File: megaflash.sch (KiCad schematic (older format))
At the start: 26 parts, among them J1 ROM7, J2 ROM0, J3 CPC_EXTPORT, U1 74LS374, U2 74LS32, U3 74LS32, U4 74LS02, U5 74LS20, U6 W29C040

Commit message: Nearly finished layout, tweaks/fixes on schematic.
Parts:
- R1: renamed from 1K1; value R -> 1K
- gave numbers to parts that had none: 1
- renumbered U3 to U2, U2 to U3
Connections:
- net labels added: ~CE, ~IORQ, ~MREQ, ~ROM0DECODE, ~ROM0SEL, ~ROM7DECODE, ~ROM7SEL, ~ROMEN, ~WR, ~WREN
- net labels removed: /CE, /ROM0DECODE, /ROM0SEL, /ROM7DECODE, /ROM7SEL, IORQ, MREQ, ROMEN, WR, WREN
- wire segments 156 -> 159
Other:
- note added: "~ROM0DECODE~ <- A14+A15+A16+A17+A18 (&0000-&3FFF)\n~ROM7DECODE~ <- ~A14~+~A15~+~A16~+A17+A18 (&1C000-&1FFFF)"
- note removed: "/ROM0DECODE <- A14+A15+A16+A17+A18 (&0000-&3FFF)\n/ROM7DECODE <- !A14+!A15+!A16+A17+A18 (&1C000-&1FFFF)"
- moved on the sheet: U3A, U3B

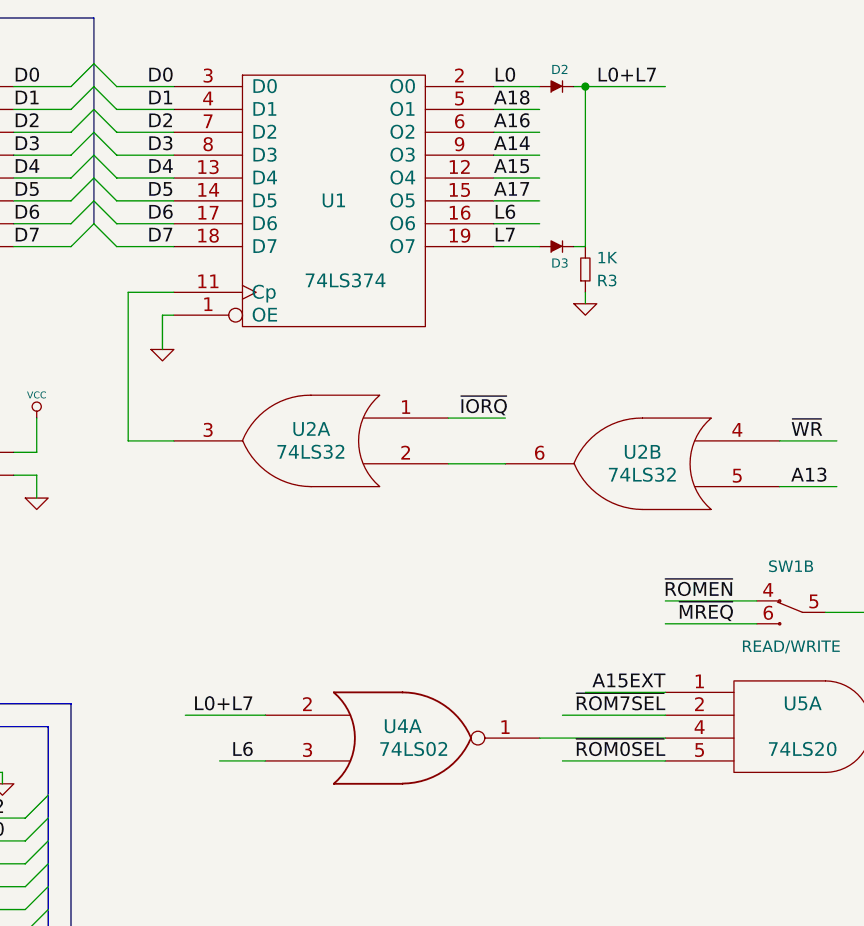
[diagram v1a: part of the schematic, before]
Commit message: Fixed scrambled latch inputs. Board mostly routed.
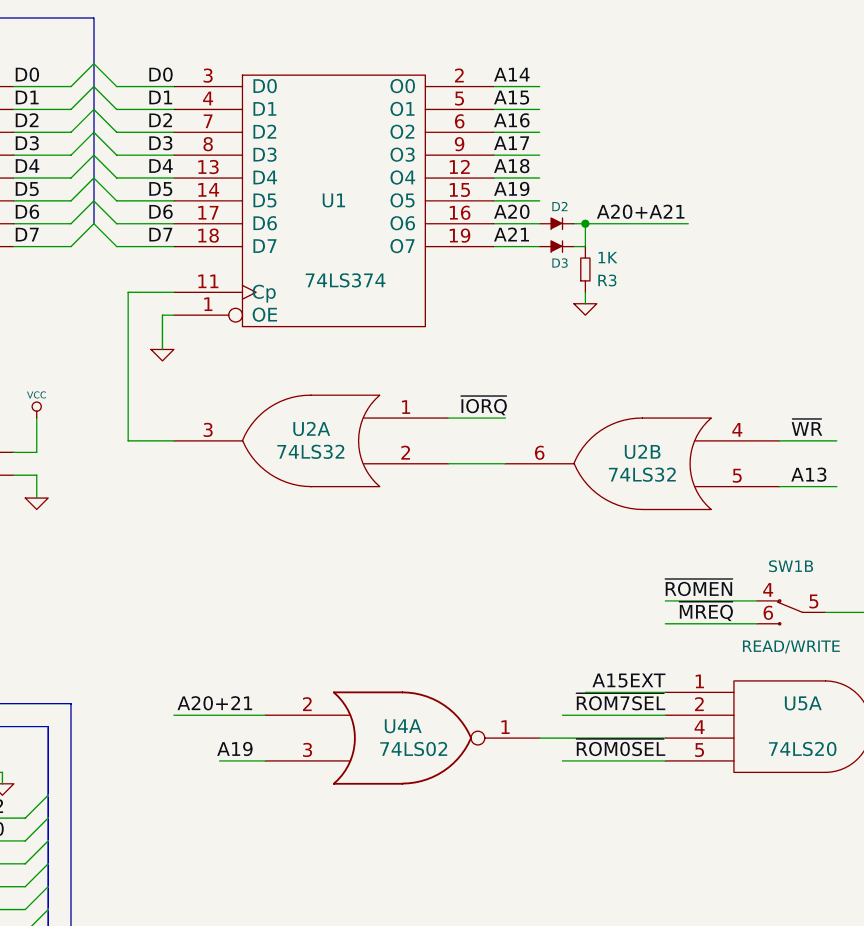
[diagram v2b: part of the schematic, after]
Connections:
- net labels added: A19, A20, A20+21, A20+A21, A21
- net labels removed: L0, L0+L7, L6, L7
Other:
- moved on the sheet: D2
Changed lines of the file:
@@
 A15EXT
 Text Label 5100 1150 0    60   ~ 0
-L0
+A14
 Text Label 5100 1250 0    60   ~ 0
-A18
+A15
 Text Label 5100 1350 0    60   ~ 0
 A16
 Text Label 5100 1450 0    60   ~ 0
-A14
+A17
 Text Label 5100 1550 0    60   ~ 0
-A15
+A18
 Text Label 5100 1650 0    60   ~ 0
-A17
+A19
 Text Label 5100 1750 0    60   ~ 0
-L6
+A20
 Text Label 5100 1850 0    60   ~ 0
-L7
+A21
 Text Label 5400 5000 2    60   ~ 0
 A17
@@
 A17
 Text Label 4050 4100 2    60   ~ 0
-L6
+A19
 Text Label 4050 3900 2    60   ~ 0
-L0+L7
+A20+21
 $Comp
 L DIODE D2
 U 1 1 534FD423
-P 5350 1150
-F 0 "D2" H 5350 1200 40  0000 L BNN
-F 1 "DIODE" H 5350 1050 40  0001 C CNN
-F 2 "" H 5350 1150 60  0000 C CNN
-F 3 "" H 5350 1150 60  0000 C CNN
-	1    5350 1150
+P 5350 1750
+F 0 "D2" H 5350 1800 40  0000 L BNN
+F 1 "DIODE" H 5350 1650 40  0001 C CNN
+F 2 "" H 5350 1750 60  0000 C CNN
+F 3 "" H 5350 1750 60  0000 C CNN
+	1    5350 1750
 	1    0    0    -1
 $EndComp
@@
 	1    0    0    -1
 $EndComp
-Text Label 5550 1150 0    60   ~ 0
-L0+L7
+Text Label 5550 1750 0    60   ~ 0
+A20+A21
 $Comp
 L R R3
@@
 	4100 4100 3900 4100
 Wire Wire Line
-	3750 3900 4100 3900
+	3700 3900 4100 3900
 Wire Wire Line
 	5450 1850 5500 1850
-Wire Wire Line
-	5500 1850 5500 1150
-Wire Wire Line
-	5450 1150 5850 1150
-Connection ~ 5500 1150
 Wire Wire Line
 	6650 5600 6850 5600
@@
 Wire Wire Line
 	2950 4150 2950 4200
-Wire Wire Line
-	4850 6950 4700 6950
 $Comp
 L LED LD1
@@
 Connection ~ 8900 1350
 Connection ~ 9200 1350
+Wire Wire Line
+	4850 6950 4700 6950
+Wire Wire Line
+	5500 1850 5500 1750
+Wire Wire Line
+	5450 1750 5950 1750
+Connection ~ 5500 1750
 $EndSCHEMATC

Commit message: Completed v1 schematic and layout using XC9536 cpld.
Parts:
- removed C1: 100u, symbol C
- removed C6, C7, C8: 100n, symbol C
- removed J1: ROM7, symbol HEADER_3
- removed J2: ROM0, symbol HEADER_3
- removed R4: 1K, symbol R
- removed SW1: READ/WRITE, symbol SW_DPDT
- removed U1: 74LS374, symbol 74LS374
- removed U2, U3: 74LS32, symbol 74LS32
- removed U4: 74LS02, symbol 74LS02
- removed U5: 74LS20, symbol 74LS20
- added C1: 100u, symbol CAP
- added C4: 10n, symbol C
- added J2: PROG, symbol HEADER_2X2
- added J3: JTAG, symbol HEADER_6
- added SW1: ~READ~/WRITE, symbol SWITCH_INV
- added SW2: ROM0ENABLE, symbol SWITCH_INV
- added SW3: ROM7ENABLE, symbol SWITCH_INV
- added U2: XC9536PC44, symbol XC9536PC44
- C2: renamed from C3; value 100n -> 10n
- C3: renamed from C4; value 100n -> 10n
- C5: value 100n -> 10n
- R2: value 220 -> 10k
- R3: value 1K -> 1k
- U1: renamed from U6; value W29C040 -> W29C040 or SST39V040
- renumbered J3 to J1
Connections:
- net labels added: A14EXT, CLK, ROM0EN, ROM7EN, ~RD, ~RD~WR
- net labels removed: A19, A20, A20+21, A20+A21, A21, ~ROM0DECODE, ~ROM0SEL, ~ROM7DECODE, ~ROM7SEL
- wire segments 159 -> 144
- no-connect marks 20 -> 16
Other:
- note removed: "~ROM0DECODE~ <- A14+A15+A16+A17+A18 (&0000-&3FFF)\n~ROM7DECODE~ <- ~A14~+~A15~+~A16~+A17+A18 (&1C000-&1FFFF)"
- moved on the sheet: C2, C3

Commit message: Replaced switch with one that's available from digikey.
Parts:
- added R4: 10k, symbol R
- R1: value 1K -> 1k
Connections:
- wire segments 144 -> 146
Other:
- moved on the sheet: LD1, R3
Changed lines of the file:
@@
 ~ROMEN
 $Comp
-L GND #PWR01
+L GND #PWR6
 U 1 1 534FA3BF
 P 3100 2950
-F 0 "#PWR01" H 3100 2950 30  0001 C CNN
+F 0 "#PWR6" H 3100 2950 30  0001 C CNN
 F 1 "GND" H 3100 2880 30  0001 C CNN
 F 2 "" H 3100 2950 60  0000 C CNN
@@
 $EndComp
 $Comp
-L VCC #PWR02
+L VCC #PWR5
 U 1 1 534FA42A
 P 3100 2600
-F 0 "#PWR02" H 3100 2700 30  0001 C CNN
+F 0 "#PWR5" H 3100 2700 30  0001 C CNN
 F 1 "VCC" H 3100 2700 30  0000 C CNN
 F 2 "" H 3100 2600 60  0000 C CNN
@@
 P 1400 6000
 F 0 "R1" H 1350 5950 50  0000 R CNN
-F 1 "1K" H 1350 6050 50  0000 R CNN
+F 1 "1k" H 1350 6050 50  0000 R CNN
 F 2 "" H 1400 6000 60  0000 C CNN
 F 3 "" H 1400 6000 60  0000 C CNN
@@
 ROMDIS
 $Comp
-L VCC #PWR03
+L VCC #PWR1
 U 1 1 534FE519
 P 1250 5550
-F 0 "#PWR03" H 1250 5650 30  0001 C CNN
+F 0 "#PWR1" H 1250 5650 30  0001 C CNN
 F 1 "VCC" H 1250 5650 30  0000 C CNN
 F 2 "" H 1250 5550 60  0000 C CNN
@@
 NoConn ~ 1800 5550
 $Comp
-L GND #PWR04
+L GND #PWR3
 U 1 1 534FFC5A
 P 1800 6600
-F 0 "#PWR04" H 1800 6600 30  0001 C CNN
+F 0 "#PWR3" H 1800 6600 30  0001 C CNN
 F 1 "GND" H 1800 6530 30  0001 C CNN
 F 2 "" H 1800 6600 60  0000 C CNN
@@
 $EndComp
 $Comp
-L GND #PWR05
+L GND #PWR4
 U 1 1 534FFDA2
 P 2950 4100
-F 0 "#PWR05" H 2950 4100 30  0001 C CNN
+F 0 "#PWR4" H 2950 4100 30  0001 C CNN
 F 1 "GND" H 2950 4030 30  0001 C CNN
 F 2 "" H 2950 4100 60  0000 C CNN
@@
 $EndComp
 $Comp
-L GND #PWR06
+L GND #PWR2
 U 1 1 53501BF6
 P 1250 5800
-F 0 "#PWR06" H 1250 5800 30  0001 C CNN
+F 0 "#PWR2" H 1250 5800 30  0001 C CNN
 F 1 "GND" H 1250 5730 30  0001 C CNN
 F 2 "" H 1250 5800 60  0000 C CNN
@@
 $EndComp
 $Comp
-L GND #PWR07
+L GND #PWR10
 U 1 1 535025BB
 P 6950 1750
-F 0 "#PWR07" H 6950 1750 30  0001 C CNN
+F 0 "#PWR10" H 6950 1750 30  0001 C CNN
 F 1 "GND" H 6950 1680 30  0001 C CNN
 F 2 "" H 6950 1750 60  0000 C CNN
@@
 $EndComp
 $Comp
-L GND #PWR08
+L GND #PWR8
 U 1 1 535363D7
 P 6400 5400
-F 0 "#PWR08" H 6400 5400 30  0001 C CNN
+F 0 "#PWR8" H 6400 5400 30  0001 C CNN
 F 1 "GND" H 6400 5330 30  0001 C CNN
 F 2 "" H 6400 5400 60  0000 C CNN
@@
 ROM7EN
 $Comp
-L GND #PWR09
+L GND #PWR16
 U 1 1 5353B454
 P 10550 2900
-F 0 "#PWR09" H 10550 2900 30  0001 C CNN
+F 0 "#PWR16" H 10550 2900 30  0001 C CNN
 F 1 "GND" H 10550 2830 30  0001 C CNN
 F 2 "" H 10550 2900 60  0000 C CNN
@@
 $EndComp
 $Comp
-L VCC #PWR010
+L VCC #PWR17
 U 1 1 5353B472
 P 10700 1650
-F 0 "#PWR010" H 10700 1750 30  0001 C CNN
+F 0 "#PWR17" H 10700 1750 30  0001 C CNN
 F 1 "VCC" H 10700 1750 30  0000 C CNN
 F 2 "" H 10700 1650 60  0000 C CNN
@@
 L LED LD1
 U 1 1 5353B7F4
-P 10050 1250
-F 0 "LD1" H 10050 1350 40  0000 C CNN
-F 1 "RED" H 10050 1150 40  0000 C CNN
-F 2 "" H 10050 1250 60  0000 C CNN
-F 3 "" H 10050 1250 60  0000 C CNN
-	1    10050 1250
-	1    0    0    -1
-$EndComp
-Text Label 9600 1250 0    60   ~ 0
+P 10050 800
+F 0 "LD1" H 10050 900 40  0000 C CNN
+F 1 "RED" H 10050 700 40  0000 C CNN
+F 2 "" H 10050 800 60  0000 C CNN
+F 3 "" H 10050 800 60  0000 C CNN
+	1    10050 800
+	1    0    0    -1
+$EndComp
+Text Label 9600 800  0    60   ~ 0
 ~RD~WR
 $Comp
 L R R3
 U 1 1 5353B81E
-P 10250 1250
-F 0 "R3" V 10200 1250 50  0000 C CNN
-F 1 "1k" V 10300 1250 50  0000 C CNN
-F 2 "" H 10250 1250 60  0000 C CNN
-F 3 "" H 10250 1250 60  0000 C CNN
-	1    10250 1250
+P 10250 800
+F 0 "R3" V 10200 800 50  0000 C CNN
+F 1 "1k" V 10300 800 50  0000 C CNN
+F 2 "" H 10250 800 60  0000 C CNN
+F 3 "" H 10250 800 60  0000 C CNN
+	1    10250 800
 	0    1    1    0
 $EndComp
 $Comp
-L GND #PWR011
+L GND #PWR15
 U 1 1 5353B82D
-P 10450 1350
-F 0 "#PWR011" H 10450 1350 30  0001 C CNN
-F 1 "GND" H 10450 1280 30  0001 C CNN
-F 2 "" H 10450 1350 60  0000 C CNN
-F 3 "" H 10450 1350 60  0000 C CNN
-	1    10450 1350
+P 10450 900
+F 0 "#PWR15" H 10450 900 30  0001 C CNN
+F 1 "GND" H 10450 830 30  0001 C CNN
+F 2 "" H 10450 900 60  0000 C CNN
+F 3 "" H 10450 900 60  0000 C CNN
+	1    10450 900
 	1    0    0    -1
 $EndComp
@@
 A18
 $Comp
-L VCC #PWR012
+L VCC #PWR7
 U 1 1 5353BDA8
 P 6350 1450
-F 0 "#PWR012" H 6350 1550 30  0001 C CNN
+F 0 "#PWR7" H 6350 1550 30  0001 C CNN
 F 1 "VCC" H 6350 1550 30  0000 C CNN
 F 2 "" H 6350 1450 60  0000 C CNN
@@
 $EndComp
 $Comp
-L VCC #PWR013
+L VCC #PWR9
 U 1 1 5353BDB7
 P 6950 1500
-F 0 "#PWR013" H 6950 1600 30  0001 C CNN
+F 0 "#PWR9" H 6950 1600 30  0001 C CNN
 F 1 "VCC" H 6950 1600 30  0000 C CNN
 F 2 "" H 6950 1500 60  0000 C CNN
@@
 $EndComp
 $Comp
-L PWR_FLAG #FLG014
+L PWR_FLAG #FLG1
 U 1 1 5353BDC6
 P 950 5550
-F 0 "#FLG014" H 950 5820 30  0001 C CNN
+F 0 "#FLG1" H 950 5820 30  0001 C CNN
 F 1 "PWR_FLAG" H 950 5780 30  0000 C CNN
 F 2 "" H 950 5550 60  0000 C CNN
@@
 	9050 2650 9450 2650
 Wire Wire Line
-	10450 1350 10450 1250
-Wire Wire Line
-	10450 1250 10350 1250
-Wire Wire Line
-	9600 1250 10000 1250
+	10450 900  10450 800
+Wire Wire Line
+	10450 800  10350 800
+Wire Wire Line
+	9600 800  10000 800
 Wire Wire Line
 	7550 2350 7950 2350
@@
 $EndComp
 $Comp
-L VCC #PWR016
+L VCC #PWR11
 U 1 1 53552269
 P 8000 5150
-F 0 "#PWR016" H 8000 5250 30  0001 C CNN
+F 0 "#PWR11" H 8000 5250 30  0001 C CNN
 F 1 "VCC" H 8000 5250 30  0000 C CNN
 F 2 "" H 8000 5150 60  0000 C CNN
@@
 $EndComp
 $Comp
-L GND #PWR017
+L GND #PWR12
 U 1 1 53552278
 P 8350 5350
-F 0 "#PWR017" H 8350 5350 30  0001 C CNN
+F 0 "#PWR12" H 8350 5350 30  0001 C CNN
 F 1 "GND" H 8350 5280 30  0001 C CNN
 F 2 "" H 8350 5350 60  0000 C CNN
@@
 	8600 4550 8600 4250
 $Comp
-L VCC #PWR?
+L VCC #PWR13
 U 1 1 53566126
 P 8600 4000
-F 0 "#PWR?" H 8600 4100 30  0001 C CNN
+F 0 "#PWR13" H 8600 4100 30  0001 C CNN
 F 1 "VCC" H 8600 4100 30  0000 C CNN
 F 2 "" H 8600 4000 60  0000 C CNN
@@
 Connection ~ 8600 4400
 Connection ~ 8600 4550
+$Comp
+L R R4
+U 1 1 53568673
+P 9900 1050
+F 0 "R4" H 9850 1000 50  0000 R CNN
+F 1 "10k" H 9850 1050 50  0000 R BNN
+F 2 "" H 9900 1050 60  0000 C CNN
+F 3 "" H 9900 1050 60  0000 C CNN
+	1    9900 1050
+	1    0    0    -1
+$EndComp
+$Comp
+L GND #PWR14
+U 1 1 535686A5
+P 9900 1250
+F 0 "#PWR14" H 9900 1250 30  0001 C CNN
+F 1 "GND" H 9900 1180 30  0001 C CNN
+F 2 "" H 9900 1250 60  0000 C CNN
+F 3 "" H 9900 1250 60  0000 C CNN
+	1    9900 1250
+	1    0    0    -1
+$EndComp
+Wire Wire Line
+	9900 950  9900 800
+Connection ~ 9900 800
+Wire Wire Line
+	9900 1250 9900 1150
 $EndSCHEMATC

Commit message: Switch to the 3.3v XC9536XL (since the 5v XC9536 is unavailable)
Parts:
- added C6, C7: 1u, symbol C
- added U3: TLV70033, symbol MIC5205
- U2: value XC9536PC44 -> XC9536XLPC44
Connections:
- net labels added: +3.3V
- wire segments 146 -> 156
- no-connect marks 16 -> 17
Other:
- moved on the sheet: C4, C5
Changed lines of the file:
@@
 $EndComp
 $Comp
-L GND #PWR10
+L GND #PWR14
 U 1 1 535025BB
 P 6950 1750
-F 0 "#PWR10" H 6950 1750 30  0001 C CNN
+F 0 "#PWR14" H 6950 1750 30  0001 C CNN
 F 1 "GND" H 6950 1680 30  0001 C CNN
 F 2 "" H 6950 1750 60  0000 C CNN
@@
 $EndComp
 $Comp
-L GND #PWR8
+L GND #PWR12
 U 1 1 535363D7
 P 6400 5400
-F 0 "#PWR8" H 6400 5400 30  0001 C CNN
+F 0 "#PWR12" H 6400 5400 30  0001 C CNN
 F 1 "GND" H 6400 5330 30  0001 C CNN
 F 2 "" H 6400 5400 60  0000 C CNN
@@
 ROM7EN
 $Comp
-L GND #PWR16
+L GND #PWR20
 U 1 1 5353B454
 P 10550 2900
-F 0 "#PWR16" H 10550 2900 30  0001 C CNN
+F 0 "#PWR20" H 10550 2900 30  0001 C CNN
 F 1 "GND" H 10550 2830 30  0001 C CNN
 F 2 "" H 10550 2900 60  0000 C CNN
@@
 $EndComp
 $Comp
-L VCC #PWR17
+L VCC #PWR21
 U 1 1 5353B472
 P 10700 1650
-F 0 "#PWR17" H 10700 1750 30  0001 C CNN
+F 0 "#PWR21" H 10700 1750 30  0001 C CNN
 F 1 "VCC" H 10700 1750 30  0000 C CNN
 F 2 "" H 10700 1650 60  0000 C CNN
@@
 $EndComp
 $Comp
-L GND #PWR15
+L GND #PWR19
 U 1 1 5353B82D
 P 10450 900
-F 0 "#PWR15" H 10450 900 30  0001 C CNN
+F 0 "#PWR19" H 10450 900 30  0001 C CNN
 F 1 "GND" H 10450 830 30  0001 C CNN
 F 2 "" H 10450 900 60  0000 C CNN
@@
 A18
 $Comp
-L VCC #PWR7
-U 1 1 5353BDA8
-P 6350 1450
-F 0 "#PWR7" H 6350 1550 30  0001 C CNN
-F 1 "VCC" H 6350 1550 30  0000 C CNN
-F 2 "" H 6350 1450 60  0000 C CNN
-F 3 "" H 6350 1450 60  0000 C CNN
-	1    6350 1450
-	1    0    0    -1
-$EndComp
-$Comp
-L VCC #PWR9
-U 1 1 5353BDB7
-P 6950 1500
-F 0 "#PWR9" H 6950 1600 30  0001 C CNN
-F 1 "VCC" H 6950 1600 30  0000 C CNN
-F 2 "" H 6950 1500 60  0000 C CNN
-F 3 "" H 6950 1500 60  0000 C CNN
-	1    6950 1500
-	1    0    0    -1
-$EndComp
-$Comp
 L PWR_FLAG #FLG1
 U 1 1 5353BDC6
@@
 L C C4
 U 1 1 5353C1C8
-P 7750 1600
-F 0 "C4" H 7800 1610 50  0000 L CNN
-F 1 "10n" H 7800 1540 50  0000 L CNN
-F 2 "" H 7750 1600 60  0000 C CNN
-F 3 "" H 7750 1600 60  0000 C CNN
-	1    7750 1600
+P 3200 2750
+F 0 "C4" H 3250 2760 50  0000 L CNN
+F 1 "10n" H 3250 2690 50  0000 L CNN
+F 2 "" H 3200 2750 60  0000 C CNN
+F 3 "" H 3200 2750 60  0000 C CNN
+	1    3200 2750
 	1    0    0    -1
 $EndComp
@@
 P 6400 3450
 F 0 "U2" H 6900 4850 60  0000 C CNN
-F 1 "XC9536PC44" H 6950 2001 60  0000 C CNN
+F 1 "XC9536XLPC44" H 6950 2001 60  0000 C CNN
 F 2 "" H 6400 3450 60  0000 C CNN
 F 3 "" H 6400 3450 60  0000 C CNN
@@
 	3100 2950 3100 2850
 Wire Wire Line
-	3100 2850 3000 2850
+	3000 2850 3200 2850
 Wire Wire Line
 	1800 5750 1600 5750
@@
 Connection ~ 7150 1700
 Connection ~ 7450 1700
-Wire Wire Line
-	6950 1550 8050 1550
-Wire Wire Line
-	6950 1700 8050 1700
 Wire Wire Line
 	6350 1850 6550 1850
@@
 $EndComp
 $Comp
-L VCC #PWR11
+L VCC #PWR15
 U 1 1 53552269
 P 8000 5150
-F 0 "#PWR11" H 8000 5250 30  0001 C CNN
+F 0 "#PWR15" H 8000 5250 30  0001 C CNN
 F 1 "VCC" H 8000 5250 30  0000 C CNN
 F 2 "" H 8000 5150 60  0000 C CNN
@@
 $EndComp
 $Comp
-L GND #PWR12
+L GND #PWR16
 U 1 1 53552278
 P 8350 5350
-F 0 "#PWR12" H 8350 5350 30  0001 C CNN
+F 0 "#PWR16" H 8350 5350 30  0001 C CNN
 F 1 "GND" H 8350 5280 30  0001 C CNN
 F 2 "" H 8350 5350 60  0000 C CNN
@@
 L C C5
 U 1 1 535644FA
-P 8050 1600
-F 0 "C5" H 8100 1610 50  0000 L CNN
-F 1 "10n" H 8100 1540 50  0000 L CNN
-F 2 "" H 8050 1600 60  0000 C CNN
-F 3 "" H 8050 1600 60  0000 C CNN
-	1    8050 1600
-	1    0    0    -1
-$EndComp
-Connection ~ 7750 1550
-Connection ~ 7750 1700
+P 7750 1600
+F 0 "C5" H 7800 1610 50  0000 L CNN
+F 1 "10n" H 7800 1540 50  0000 L CNN
+F 2 "" H 7750 1600 60  0000 C CNN
+F 3 "" H 7750 1600 60  0000 C CNN
+	1    7750 1600
+	1    0    0    -1
+$EndComp
 $Comp
 L CAP C1
@@
 	8600 4550 8600 4250
 $Comp
-L VCC #PWR13
+L VCC #PWR17
 U 1 1 53566126
 P 8600 4000
-F 0 "#PWR13" H 8600 4100 30  0001 C CNN
+F 0 "#PWR17" H 8600 4100 30  0001 C CNN
 F 1 "VCC" H 8600 4100 30  0000 C CNN
 F 2 "" H 8600 4000 60  0000 C CNN
@@
 $EndComp
 $Comp
-L GND #PWR14
+L GND #PWR18
 U 1 1 535686A5
 P 9900 1250
-F 0 "#PWR14" H 9900 1250 30  0001 C CNN
+F 0 "#PWR18" H 9900 1250 30  0001 C CNN
 F 1 "GND" H 9900 1180 30  0001 C CNN
 F 2 "" H 9900 1250 60  0000 C CNN
@@
 Wire Wire Line
 	9900 1250 9900 1150
+$Comp
+L +3.3V #PWR9
+U 1 1 53579090
+P 5800 1200
+F 0 "#PWR9" H 5800 1160 30  0001 C CNN
+F 1 "+3.3V" H 5800 1310 30  0000 C CNN
+F 2 "" H 5800 1200 60  0000 C CNN
+F 3 "" H 5800 1200 60  0000 C CNN
+	1    5800 1200
+	1    0    0    -1
+$EndComp
+Wire Wire Line
+	5800 1200 5700 1200
+Connection ~ 3100 2850
+Wire Wire Line
+	3200 2700 3100 2700
+Connection ~ 3100 2700
+$Comp
+L +3.3V #PWR13
+U 1 1 535792C2
+P 6950 1500
+F 0 "#PWR13" H 6950 1460 30  0001 C CNN
+F 1 "+3.3V" H 6950 1610 30  0000 C CNN
+F 2 "" H 6950 1500 60  0000 C CNN
+F 3 "" H 6950 1500 60  0000 C CNN
+	1    6950 1500
+	1    0    0    -1
+$EndComp
+$Comp
+L +3.3V #PWR11
+U 1 1 535792D1
+P 6350 1450
+F 0 "#PWR11" H 6350 1410 30  0001 C CNN
+F 1 "+3.3V" H 6350 1560 30  0000 C CNN
+F 2 "" H 6350 1450 60  0000 C CNN
+F 3 "" H 6350 1450 60  0000 C CNN
+	1    6350 1450
+	1    0    0    -1
+$EndComp
+Wire Wire Line
+	6950 1700 7750 1700
+Wire Wire Line
+	6950 1550 7750 1550
+$Comp
+L VCC #PWR7
+U 1 1 535795AD
+P 4300 1100
+F 0 "#PWR7" H 4300 1200 30  0001 C CNN
+F 1 "VCC" H 4300 1200 30  0000 C CNN
+F 2 "" H 4300 1100 60  0000 C CNN
+F 3 "" H 4300 1100 60  0000 C CNN
+	1    4300 1100
+	1    0    0    -1
+$EndComp
+Wire Wire Line
+	4300 1200 4550 1200
+$Comp
+L GND #PWR8
+U 1 1 53579670
+P 4300 1500
+F 0 "#PWR8" H 4300 1500 30  0001 C CNN
+F 1 "GND" H 4300 1430 30  0001 C CNN
+F 2 "" H 4300 1500 60  0000 C CNN
+F 3 "" H 4300 1500 60  0000 C CNN
+	1    4300 1500
+	1    0    0    -1
+$EndComp
+Wire Wire Line
+	4550 1350 4300 1350
+Wire Wire Line
+	4550 1500 4450 1500
+Wire Wire Line
+	4450 1500 4450 1200
+$Comp
+L GND #PWR10
+U 1 1 53579972
+P 5800 1550
+F 0 "#PWR10" H 5800 1550 30  0001 C CNN
+F 1 "GND" H 5800 1480 30  0001 C CNN
+F 2 "" H 5800 1550 60  0000 C CNN
+F 3 "" H 5800 1550 60  0000 C CNN
+	1    5800 1550
+	1    0    0    -1
+$EndComp
+Wire Wire Line
+	5800 1450 5800 1550
+$Comp
+L MIC5205 U3
+U 1 1 53579081
+P 5100 1350
+F 0 "U3" H 4900 1650 60  0000 C CNN
+F 1 "TLV70033" H 5200 1050 60  0000 C CNN
+F 2 "" H 5100 1350 60  0000 C CNN
+F 3 "" H 5100 1350 60  0000 C CNN
+	1    5100 1350
+	1    0    0    -1
+$EndComp
+NoConn ~ 5700 1500
+Wire Wire Line
+	5800 1300 5800 1200
+$Comp
+L C C7
+U 1 1 53579E7C
+P 5800 1350
+F 0 "C7" H 5850 1360 50  0000 L CNN
+F 1 "1u" H 5850 1290 50  0000 L CNN
+F 2 "" H 5800 1350 60  0000 C CNN
+F 3 "" H 5800 1350 60  0000 C CNN
+	1    5800 1350
+	1    0    0    -1
+$EndComp
+$Comp
+L C C6
+U 1 1 53579E8B
+P 4300 1300
+F 0 "C6" H 4350 1310 50  0000 L CNN
+F 1 "1u" H 4350 1240 50  0000 L CNN
+F 2 "" H 4300 1300 60  0000 C CNN
+F 3 "" H 4300 1300 60  0000 C CNN
+	1    4300 1300
+	-1   0    0    1
+$EndComp
+Connection ~ 4450 1200
+Wire Wire Line
+	4300 1200 4300 1100
+Wire Wire Line
+	4300 1350 4300 1500
 $EndSCHEMATC
